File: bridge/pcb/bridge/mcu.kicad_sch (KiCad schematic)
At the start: 16 parts, among them J11 5V_Enable, J5 Conn_01x04, J6 Conn_01x02, J7 Conn_01x03, J8 Conn_01x02, J9 MCU_Test_Point, U1 L293, U3 AD557JN, U4 ATmega328P-P, U5 L7805

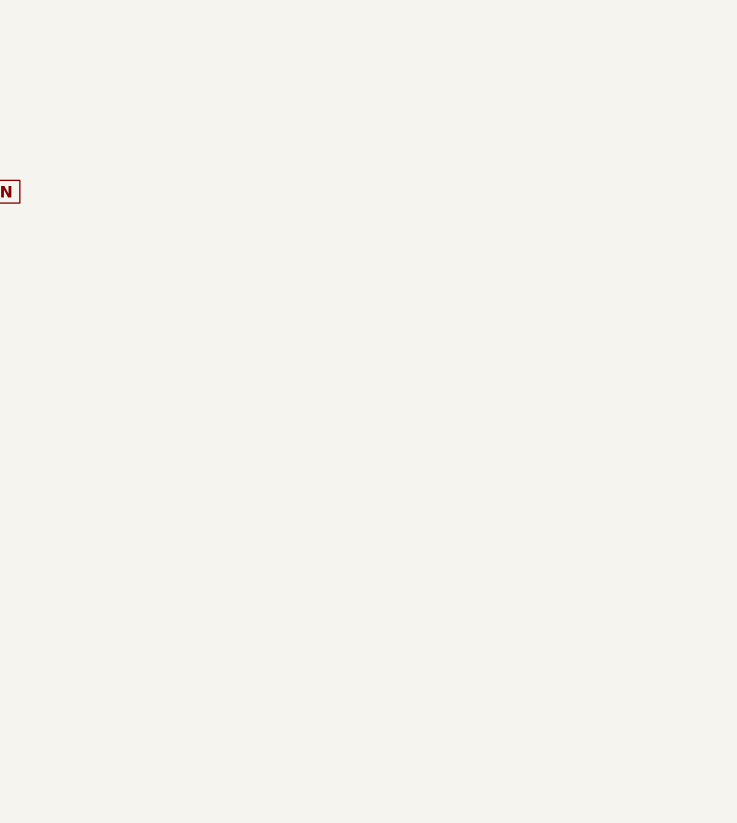
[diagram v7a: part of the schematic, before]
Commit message: Added status LED's for all of the motor controller switches
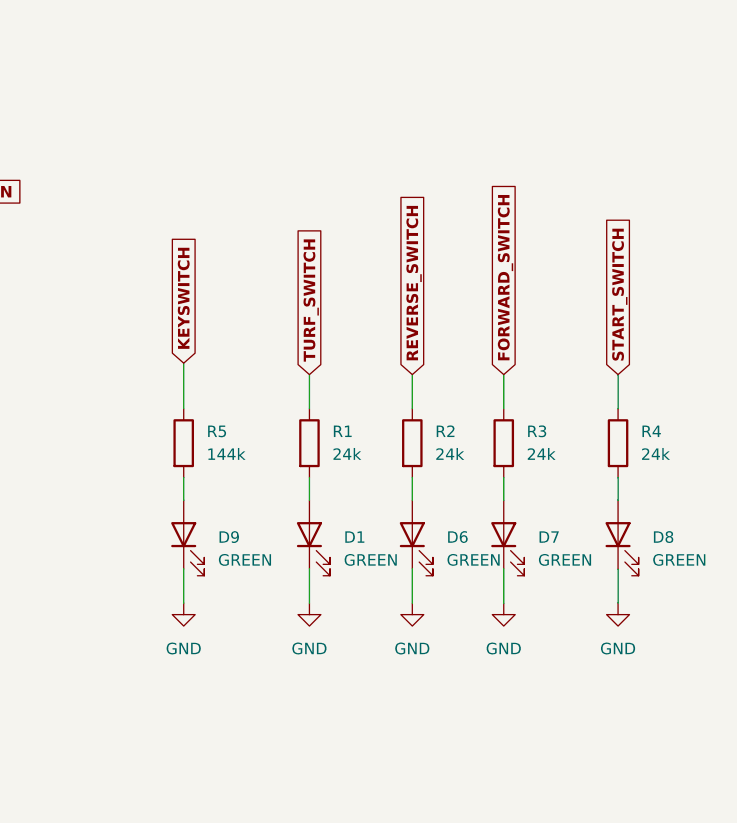
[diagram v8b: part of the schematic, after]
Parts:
- added D1, D6, D7, D8, D9: GREEN, LED_THT:LED_D5.0mm, symbol Device:LED
- added R1, R2, R3, R4: 24k, bridge:THT_RESISTOR_WITH_VALUE, symbol Device:R
- added R5: 144k, bridge:THT_RESISTOR_WITH_VALUE, symbol Device:R
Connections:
- net FORWARD_SWITCH: now also R3.1
- net GND: now also D1.1 (K), D6.1 (K), D7.1 (K), D8.1 (K), D9.1 (K)
- net KEYSWITCH: now also R5.1
- net REVERSE_SWITCH: now also R2.1
- net START_SWITCH: now also R4.1
- net TURF_SWITCH: now also R1.1
- new net: D7.2 (A), R3.2
- new net: D9.2 (A), R5.2
- new net: D8.2 (A), R4.2
- new net: D1.2 (A), R1.2
- new net: D6.2 (A), R2.2
